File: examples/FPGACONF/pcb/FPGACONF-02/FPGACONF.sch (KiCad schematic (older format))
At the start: 0 parts

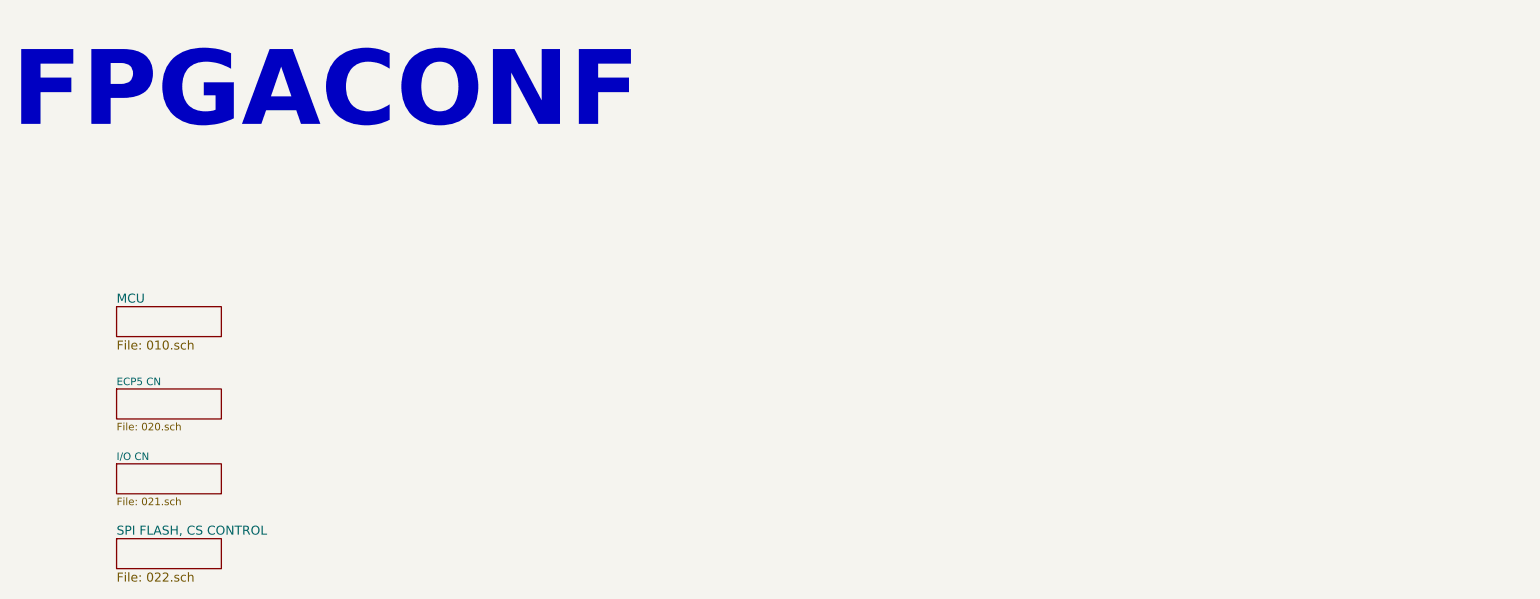
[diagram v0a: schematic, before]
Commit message: FPGACONF-02 schematics  support for SD-DDR (H743) test
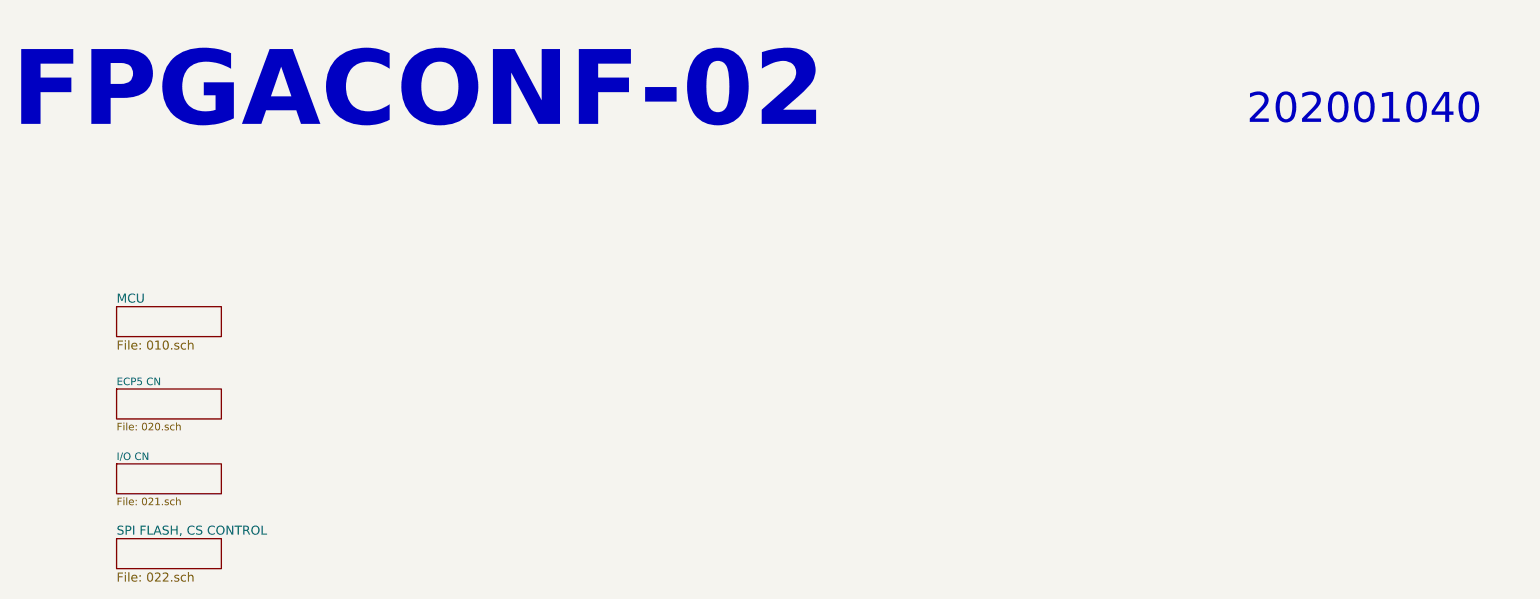
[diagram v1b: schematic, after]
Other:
- note added: "202001040"
- note added: "FPGACONF-02\n"
- note removed: "FPGACONF\n"
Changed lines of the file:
@@
 $EndDescr
 Text Notes 1900 2400 0    500  ~ 100
-FPGACONF\n
+FPGACONF-02\n
 $Sheet
 S 2600 3550 700  200
@@
 F1 "022.sch" 60
 $EndSheet
+Text Notes 10150 2350 0    200  ~ 0
+202001040
 $EndSCHEMATC
